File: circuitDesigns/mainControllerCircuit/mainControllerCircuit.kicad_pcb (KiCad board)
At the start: 2 copper layers, 125 x 99.8 mm, 49 parts, among them J1 USB_A, J2 USB_A, J3 USB_A, J4 Conn_01x15_Pin, J5 Conn_01x15_Pin, J6 Conn_01x16_Socket, J7 OutputVCC, Q1 AO3400A, Q10 AO3400A, Q11 AO3400A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

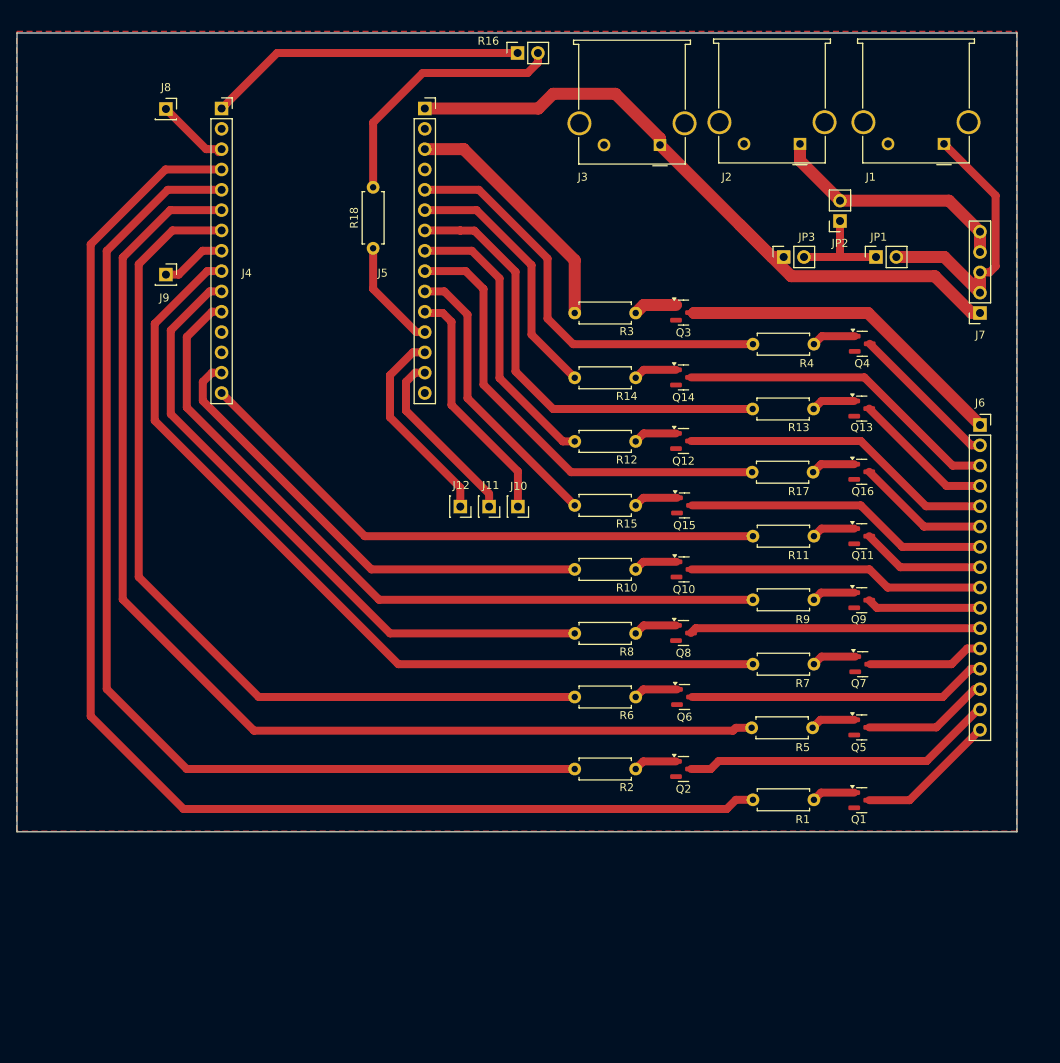
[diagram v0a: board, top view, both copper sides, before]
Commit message: Fixes error in controller circuit: mosfets were missing pull down resistor
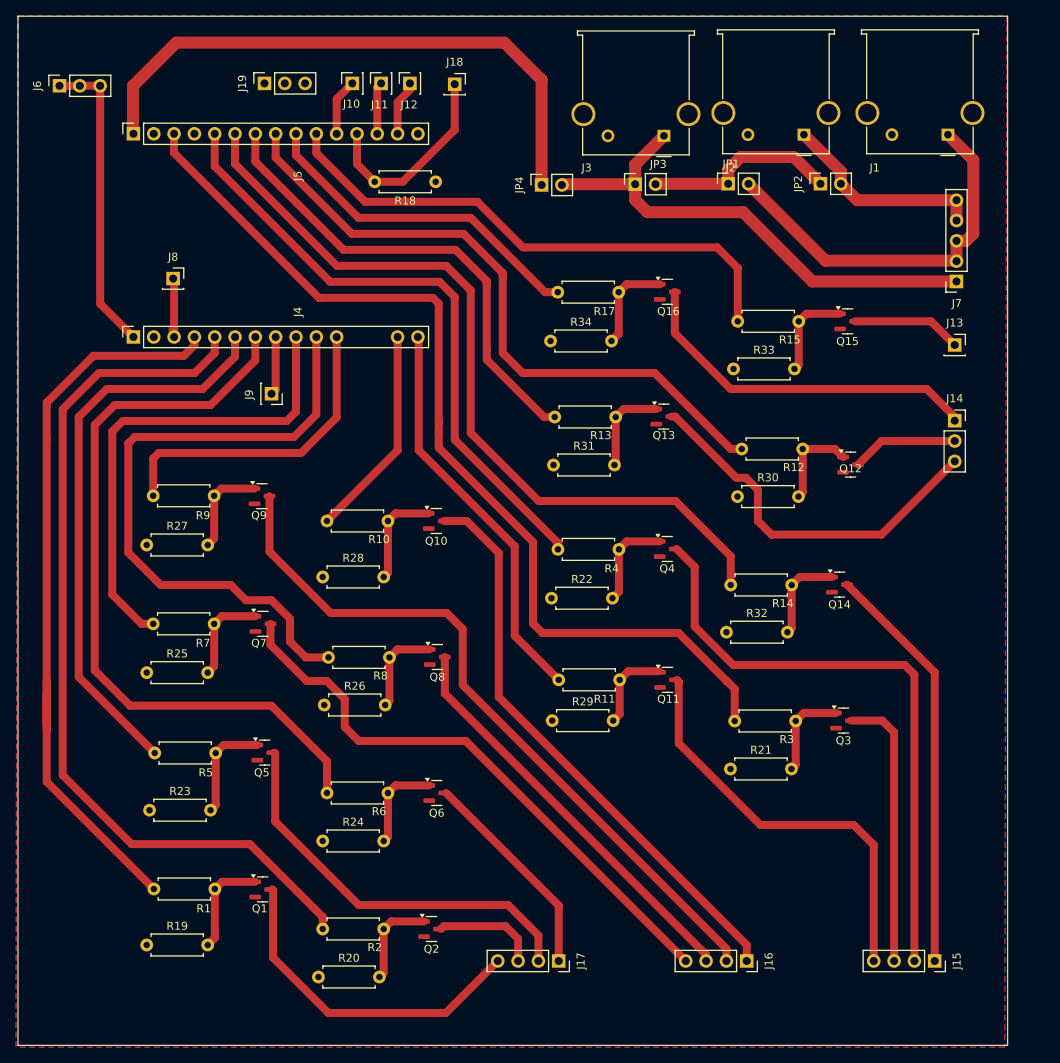
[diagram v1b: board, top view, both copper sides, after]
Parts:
- removed R16: R_Photo, Connector_PinSocket_2.54mm:PinSocket_1x02_P2.54mm_Vertical
- added J13: Moon, Connector_PinSocket_2.54mm:PinSocket_1x01_P2.54mm_Vertical, F.Cu at (269.5, 59.0)
- added J14: LS1-3, Connector_PinSocket_2.54mm:PinSocket_1x03_P2.54mm_Vertical, F.Cu at (269.5, 68.5)
- added J15: SS1-4, Connector_PinSocket_2.54mm:PinSocket_1x04_P2.54mm_Vertical, F.Cu at (267.0, 136.0)
- added J16: SS5-8, Connector_PinSocket_2.54mm:PinSocket_1x04_P2.54mm_Vertical, F.Cu at (243.5, 136.0)
- added J17: SS9-12, Connector_PinSocket_2.54mm:PinSocket_1x04_P2.54mm_Vertical, F.Cu at (220.0, 136.0)
- added J18: LightSensor, Connector_PinSocket_2.54mm:PinSocket_1x01_P2.54mm_Vertical, F.Cu at (207.0, 26.4)
- added J19: OutGND, Connector_PinSocket_2.54mm:PinSocket_1x03_P2.54mm_Vertical, F.Cu at (183.2, 26.3)
- added JP4: SolderJumper, Connector_PinSocket_2.54mm:PinSocket_1x02_P2.54mm_Vertical, F.Cu at (217.9, 39.0)
- added R19: 10K, Resistor_THT:R_Axial_DIN0207_L6.3mm_D2.5mm_P7.62mm_Horizontal, F.Cu at (168.5, 134.0)
- added R20: 10K, Resistor_THT:R_Axial_DIN0207_L6.3mm_D2.5mm_P7.62mm_Horizontal, F.Cu at (190.0, 138.0)
- added R21: 10K, Resistor_THT:R_Axial_DIN0207_L6.3mm_D2.5mm_P7.62mm_Horizontal, F.Cu at (241.5, 112.0)
- added R22: 10K, Resistor_THT:R_Axial_DIN0207_L6.3mm_D2.5mm_P7.62mm_Horizontal, F.Cu at (219.1, 90.7)
- added R23: 10K, Resistor_THT:R_Axial_DIN0207_L6.3mm_D2.5mm_P7.62mm_Horizontal, F.Cu at (168.9, 117.2)
- added R24: 10K, Resistor_THT:R_Axial_DIN0207_L6.3mm_D2.5mm_P7.62mm_Horizontal, F.Cu at (190.5, 121.0)
- added R25: 10K, Resistor_THT:R_Axial_DIN0207_L6.3mm_D2.5mm_P7.62mm_Horizontal, F.Cu at (168.5, 100.0)
- added R26: 10K, Resistor_THT:R_Axial_DIN0207_L6.3mm_D2.5mm_P7.62mm_Horizontal, F.Cu at (190.7, 104.0)
- added R27: 10K, Resistor_THT:R_Axial_DIN0207_L6.3mm_D2.5mm_P7.62mm_Horizontal, F.Cu at (168.5, 84.0)
- added R28: 10K, Resistor_THT:R_Axial_DIN0207_L6.3mm_D2.5mm_P7.62mm_Horizontal, F.Cu at (190.5, 88.0)
- added R29: 10K, Resistor_THT:R_Axial_DIN0207_L6.3mm_D2.5mm_P7.62mm_Horizontal, F.Cu at (219.2, 106.0)
- added R30: 10K, Resistor_THT:R_Axial_DIN0207_L6.3mm_D2.5mm_P7.62mm_Horizontal, F.Cu at (242.3, 78.0)
- added R31: 10K, Resistor_THT:R_Axial_DIN0207_L6.3mm_D2.5mm_P7.62mm_Horizontal, F.Cu at (219.3, 74.0)
- added R32: 10K, Resistor_THT:R_Axial_DIN0207_L6.3mm_D2.5mm_P7.62mm_Horizontal, F.Cu at (241.0, 94.9)
- added R33: 10K, Resistor_THT:R_Axial_DIN0207_L6.3mm_D2.5mm_P7.62mm_Horizontal, F.Cu at (241.8, 62.0)
- added R34: 10K, Resistor_THT:R_Axial_DIN0207_L6.3mm_D2.5mm_P7.62mm_Horizontal, F.Cu at (219.0, 58.5)
- J6: value Conn_01x16_Socket -> Out3V3; footprint Connector_PinSocket_2.54mm:PinSocket_1x16_P2.54mm_Vertical -> Connector_PinSocket_2.54mm:PinSocket_1x03_P2.54mm_Vertical
- moved J6 122.6 mm to (157.6, 26.6), turned to 90 degrees
- moved Q9 76.1 mm to (182.9, 77.9)
- moved R9 76.1 mm to (169.3, 77.8)
- moved Q1 75.7 mm to (183.0, 127.0)
- moved R1 75.7 mm to (169.4, 127.0)
- moved Q7 75.1 mm to (183.0, 93.9)
- moved R7 75.1 mm to (169.3, 93.9)
- moved Q5 74.7 mm to (183.3, 110.0)
- moved R5 74.7 mm to (169.5, 110.0)
- moved J10 56.8 mm to (194.2, 26.3), turned to 90 degrees
- moved Q3 54.8 mm to (255.6, 106.0)
- moved R3 54.8 mm to (242.0, 106.0)
- moved J11 54.6 mm to (197.8, 26.3), turned to 90 degrees
- moved J12 53.3 mm to (201.4, 26.3), turned to 90 degrees
- moved Q2 37.3 mm to (204.1, 132.0)
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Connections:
- J5 pad 1: +5V -> Net-(J5-Pin_1)
- J5 pad 12: Net-(J5-Pin_12) -> Net-(J18-Pin_1)
- J5 pad 13: Net-(J12-Pin_1) -> Net-(J11-Pin_1)
- J5 pad 14: Net-(J11-Pin_1) -> Net-(J12-Pin_1)
- J6 pad 1: Net-(J6-Pin_1) -> Net-(J4-Pin_1)
- J6 pad 2: Net-(J6-Pin_2) -> Net-(J4-Pin_1)
- J6 pad 3: Net-(J6-Pin_3) -> Net-(J4-Pin_1)
- Q1 pad 3: Net-(J6-Pin_16) -> Net-(J17-Pin_4)
- Q10 pad 3: Net-(J6-Pin_9) -> Net-(J16-Pin_1)
- Q11 pad 3: Net-(J6-Pin_8) -> Net-(J15-Pin_4)
- Q12 pad 3: Net-(J6-Pin_5) -> Net-(J14-Pin_2)
- Q13 pad 3: Net-(J6-Pin_4) -> Net-(J14-Pin_3)
- Q14 pad 3: Net-(J6-Pin_3) -> Net-(J15-Pin_1)
- Q15 pad 3: Net-(J6-Pin_7) -> Net-(J13-Pin_1)
- Q16 pad 3: Net-(J6-Pin_6) -> Net-(J14-Pin_1)
- Q2 pad 3: Net-(J6-Pin_15) -> Net-(J17-Pin_3)
- Q3 pad 3: Net-(J6-Pin_1) -> Net-(J15-Pin_3)
- Q4 pad 3: Net-(J6-Pin_2) -> Net-(J15-Pin_2)
- Q5 pad 3: Net-(J6-Pin_14) -> Net-(J17-Pin_2)
- Q6 pad 3: Net-(J6-Pin_13) -> Net-(J17-Pin_1)
- Q7 pad 3: Net-(J6-Pin_12) -> Net-(J16-Pin_4)
- Q8 pad 3: Net-(J6-Pin_11) -> Net-(J16-Pin_3)
- Q9 pad 3: Net-(J6-Pin_10) -> Net-(J16-Pin_2)
- R18 pad 1: Net-(J5-Pin_12) -> GND
- R18 pad 2: Net-(R16-Pad2) -> Net-(J18-Pin_1)
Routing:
- net Net-(J16-Pin_2): track 0.00 -> 90.3 mm
- net Net-(J5-Pin_3): track 31.1 -> 120.7 mm
- net Net-(J15-Pin_2): track 0.00 -> 76.4 mm
- net Net-(J5-Pin_1): track 0.00 -> 74.4 mm
- net Net-(J16-Pin_4): track 0.00 -> 72.9 mm
- net Net-(J16-Pin_1): track 0.00 -> 72.4 mm
- net Net-(J4-Pin_6): track 143.1 -> 71.1 mm
- net Net-(J4-Pin_4): track 167.3 -> 98.6 mm
- net Net-(J5-Pin_6): track 32.5 -> 100.1 mm
- net Net-(J4-Pin_11): track 95.2 -> 39.8 mm
- net Net-(J15-Pin_4): track 0.00 -> 52.2 mm
- net Net-(J15-Pin_1): track 0.00 -> 51.6 mm
- net Net-(J16-Pin_3): track 0.00 -> 51.5 mm
- net Net-(J17-Pin_2): track 0.00 -> 50.7 mm
- net Net-(J4-Pin_9): track 110.6 -> 60.3 mm
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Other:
- board size 125 x 99.8 mm -> 123.7 x 128.6 mm

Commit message: Adds LED indicators to the main controller board
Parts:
- added D1: LED, LED_THT:LED_D3.0mm, F.Cu at (264.4, 56.9)
- added D10: LED, LED_THT:LED_D3.0mm, F.Cu at (241.0, 129.7)
- added D11: LED, LED_THT:LED_D3.0mm, F.Cu at (236.4, 129.7)
- added D12: LED, LED_THT:LED_D3.0mm, F.Cu at (231.8, 129.7)
- added D13: LED, LED_THT:LED_D3.0mm, F.Cu at (211.7, 129.7)
- added D14: LED, LED_THT:LED_D3.0mm, F.Cu at (216.3, 129.7)
- added D15: LED, LED_THT:LED_D3.0mm, F.Cu at (220.9, 129.7)
- added D16: LED, LED_THT:LED_D3.0mm, F.Cu at (225.5, 129.7)
- added D2: LED, LED_THT:LED_D3.0mm, F.Cu at (260.9, 80.8)
- added D3: LED, LED_THT:LED_D3.0mm, F.Cu at (265.5, 80.8)
- added D4: LED, LED_THT:LED_D3.0mm, F.Cu at (270.1, 80.8)
- added D5: LED, LED_THT:LED_D3.0mm, F.Cu at (265.7, 129.6)
- added D6: LED, LED_THT:LED_D3.0mm, F.Cu at (261.1, 129.6)
- added D7: LED, LED_THT:LED_D3.0mm, F.Cu at (256.6, 129.6)
- added D8: LED, LED_THT:LED_D3.0mm, F.Cu at (252.0, 129.6)
- added D9: LED, LED_THT:LED_D3.0mm, F.Cu at (245.6, 129.7)
- added R16: 1K, Resistor_THT:R_Axial_DIN0207_L6.3mm_D2.5mm_P7.62mm_Horizontal, F.Cu at (269.7, 63.8)
- added R35: 1K, Resistor_THT:R_Axial_DIN0207_L6.3mm_D2.5mm_P7.62mm_Horizontal, F.Cu at (262.2, 94.0)
- added R36: 1K, Resistor_THT:R_Axial_DIN0207_L6.3mm_D2.5mm_P7.62mm_Horizontal, F.Cu at (265.5, 93.9)
- added R37: 1K, Resistor_THT:R_Axial_DIN0207_L6.3mm_D2.5mm_P7.62mm_Horizontal, F.Cu at (268.7, 93.9)
- added R38: 1K, Resistor_THT:R_Axial_DIN0207_L6.3mm_D2.5mm_P7.62mm_Horizontal, F.Cu at (265.7, 142.8)
- added R39: 1K, Resistor_THT:R_Axial_DIN0207_L6.3mm_D2.5mm_P7.62mm_Horizontal, F.Cu at (261.2, 142.8)
- added R40: 1K, Resistor_THT:R_Axial_DIN0207_L6.3mm_D2.5mm_P7.62mm_Horizontal, F.Cu at (256.6, 142.8)
- added R41: 1K, Resistor_THT:R_Axial_DIN0207_L6.3mm_D2.5mm_P7.62mm_Horizontal, F.Cu at (252.0, 142.8)
- added R42: 1K, Resistor_THT:R_Axial_DIN0207_L6.3mm_D2.5mm_P7.62mm_Horizontal, F.Cu at (245.6, 142.8)
- added R43: 1K, Resistor_THT:R_Axial_DIN0207_L6.3mm_D2.5mm_P7.62mm_Horizontal, F.Cu at (241.0, 142.8)
- added R44: 1K, Resistor_THT:R_Axial_DIN0207_L6.3mm_D2.5mm_P7.62mm_Horizontal, F.Cu at (236.4, 142.8)
- added R45: 1K, Resistor_THT:R_Axial_DIN0207_L6.3mm_D2.5mm_P7.62mm_Horizontal, F.Cu at (231.8, 142.8)
- added R46: 1K, Resistor_THT:R_Axial_DIN0207_L6.3mm_D2.5mm_P7.62mm_Horizontal, F.Cu at (211.7, 142.8)
- added R47: 1K, Resistor_THT:R_Axial_DIN0207_L6.3mm_D2.5mm_P7.62mm_Horizontal, F.Cu at (216.3, 142.8)
- added R48: 1K, Resistor_THT:R_Axial_DIN0207_L6.3mm_D2.5mm_P7.62mm_Horizontal, F.Cu at (220.9, 142.8)
- added R49: 1K, Resistor_THT:R_Axial_DIN0207_L6.3mm_D2.5mm_P7.62mm_Horizontal, F.Cu at (225.5, 142.8)
- moved J17 12.4 mm to (215.1, 124.6), turned to 90 degrees
- moved J15 12.1 mm to (262.7, 124.7)
- moved J16 11.5 mm to (242.8, 124.5)
- moved J14 10.2 mm to (263.0, 76.4), turned to 90 degrees
- moved J13 8.41 mm to (261.4, 56.9)
- moved R18 7.45 mm to (212.0, 37.6)
- moved Q1 2.24 mm to (182.0, 129.1)
- moved R1 2.24 mm to (168.4, 129.0)
- moved R19 2.24 mm to (167.5, 136.0)
- moved J6 1.83 mm to (157.8, 28.4), turned to 180 degrees
- moved Q5 0.50 mm to (182.8, 110.0)
- moved Q7 0.50 mm to (182.5, 93.9)
- moved R23 0.50 mm to (168.4, 117.2)
- moved R25 0.50 mm to (168.0, 100.0)
- moved R5 0.50 mm to (169.0, 110.0)
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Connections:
- net +5V renamed Net-(J3-VBUS)
- J14 pad 1: Net-(J14-Pin_1) -> Net-(D2-K)
- J14 pad 3: Net-(J14-Pin_3) -> Net-(D4-K)
- J17 pad 1: Net-(J17-Pin_1) -> Net-(D13-K)
- J17 pad 2: Net-(J17-Pin_2) -> Net-(D14-K)
- J17 pad 3: Net-(J17-Pin_3) -> Net-(D15-K)
- J17 pad 4: Net-(J17-Pin_4) -> Net-(D16-K)
- Q1 pad 3: Net-(J17-Pin_4) -> Net-(D13-K)
- Q13 pad 3: Net-(J14-Pin_3) -> Net-(D2-K)
- Q16 pad 3: Net-(J14-Pin_1) -> Net-(D4-K)
- Q2 pad 3: Net-(J17-Pin_3) -> Net-(D14-K)
- Q5 pad 3: Net-(J17-Pin_2) -> Net-(D15-K)
- Q6 pad 3: Net-(J17-Pin_1) -> Net-(D16-K)
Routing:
- net Net-(J2-VBUS): track 25.9 -> 229.0 mm
- net Net-(D13-K): track 0.00 -> 63.0 mm
- net Net-(D15-K): track 0.00 -> 59.5 mm
- net Net-(J1-VBUS): track 48.7 -> 107.0 mm
- net Net-(D4-K): track 0.00 -> 52.8 mm
- net Net-(J17-Pin_2): track 50.7 -> 0.00 mm
- net Net-(J14-Pin_3): track 47.6 -> 0.00 mm
- net Net-(D2-K): track 0.00 -> 45.2 mm
- net Net-(J14-Pin_1): track 45.0 -> 0.00 mm
- net Net-(J17-Pin_4): track 42.2 -> 0.00 mm
- net Net-(D16-K): track 0.00 -> 29.6 mm
- net Net-(D14-K): track 0.00 -> 28.5 mm
- net Net-(J17-Pin_1): track 26.8 -> 0.00 mm
- net Net-(D6-K): track 76.4 -> 62.6 mm
- net Net-(J17-Pin_3): track 13.2 -> 0.00 mm
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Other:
- board size 123.7 x 128.6 mm -> 127.6 x 128.6 mm
